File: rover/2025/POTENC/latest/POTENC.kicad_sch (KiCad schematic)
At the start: 0 parts

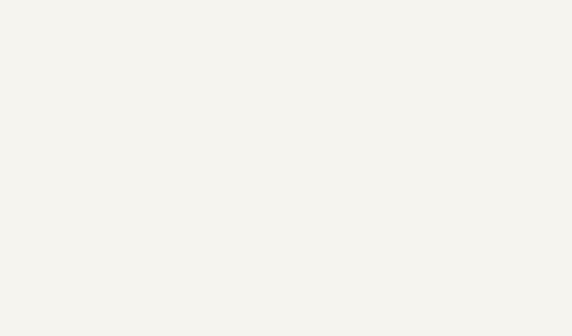
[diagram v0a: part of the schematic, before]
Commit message: ArmJ2 revised for order
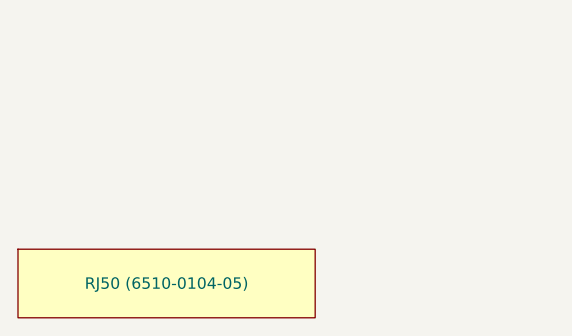
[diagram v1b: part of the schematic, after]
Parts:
- added G1: RJ50 (6510-0104-05), symbol RoverLibrary:Off Board Part
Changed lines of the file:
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@@
+		)
+	)
+	(symbol
+		(lib_name "Off Board Part_1")
+		(lib_id "RoverLibrary:Off Board Part")
+		(at 30.48 130.81 0)
+		(unit 1)
+		(exclude_from_sim yes)
+		(in_bom yes)
+		(on_board no)
+		(dnp no)
+		(fields_autoplaced yes)
+		(property "Reference" "G1"
+			(at 30.48 88.9701 0)
+			(effects
+				(font
+					(size 1.27 1.27)
+				)
+				(hide yes)
+			)
+		)
+		(property "Value" "RJ50 (6510-0104-05)"
+			(at 30.48 130.81 0)
+			(effects
+				(font
+					(size 1.27 1.27)
+				)
+			)
+		)
+		(property "Footprint" ""
+			(at 27.94 129.54 0)
+			(effects
+				(font
+					(size 1.27 1.27)
+				)
+				(hide yes)
+			)
+		)
+		(property "Datasheet" ""
+			(at 27.94 129.54 0)
+			(effects
+				(font
+					(size 1.27 1.27)
+				)
+				(hide yes)
+			)
+		)
+		(property "Description" ""
+			(at 27.94 129.54 0)
+			(effects
+				(font
+					(size 1.27 1.27)
+				)
+				(hide yes)
+			)
+		)
+		(property "Digikey" "https://www.digikey.ca/en/products/detail/encitech-connectors-ab/6510-0104-05/25596593"
+			(at 30.48 130.81 0)
+			(effects
+				(font
+					(size 1.27 1.27)
+				)
+				(hide yes)
+			)
+		)
+		(instances
+			(project "POTENC"
+				(path "/0a8240f1-1c25-4c2f-8c36-25ec707ee8f2"
+					(reference "G1")
+					(unit 1)
+				)
+			)
 		)
 	)
